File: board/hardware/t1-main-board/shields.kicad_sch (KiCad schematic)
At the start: 3 parts

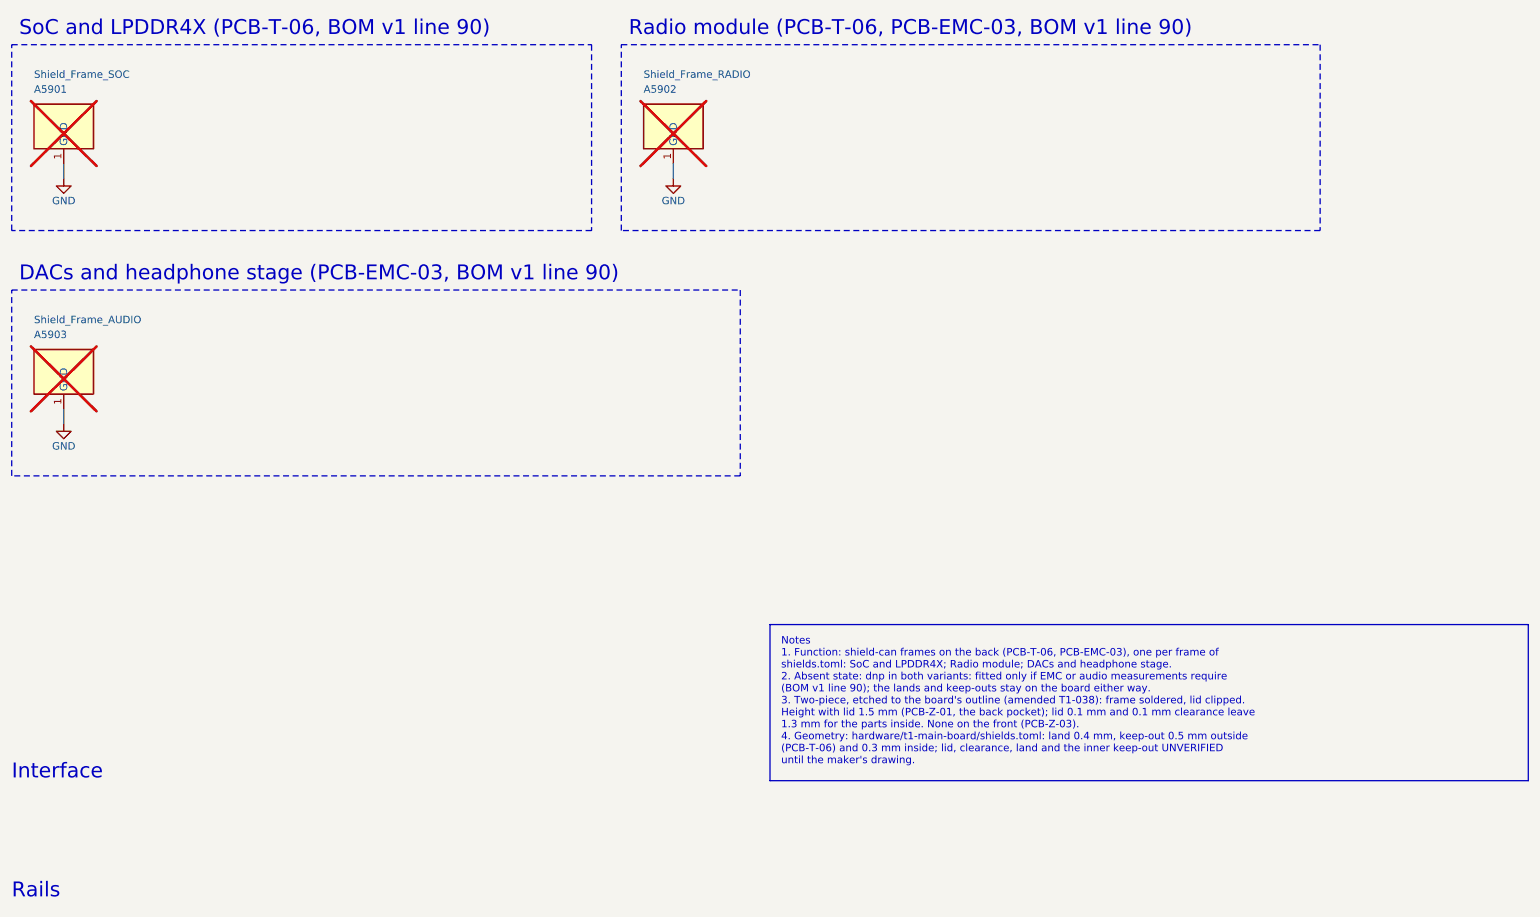
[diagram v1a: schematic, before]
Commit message: Schematic: side-pin grounds drop below their pin; shield frames in one group
A ground on an IC's side pin whose next row is taken (U1201 MODE/SYNC on
blk.vdd-cpu, U2801 VNEG/FBN on blk.hpa-rails-pre) leaves on a stub past
its neighbours' text and drops to the first free row, its GND symbol
pointing down below the pin instead of hanging among the neighbours'
labels (CRAFT-85); a ground below it on the same side joins the drop.
The shield-can frames share one group sized from its contents
(CRAFT-174) instead of three groups as wide as their titles. Other
sheets change only in #PWR numbering.

Generated twice, identical. ERC 0 errors (9 warnings, as before), craft
Q1 met (Q2 reached), overlaps 0 collisions; both sheets checked on
200 dpi PDF crops. References unchanged, so the board is not rebuilt.

Co-Authored-By: Claude Opus 5.5 <noreply@anthropic.com>
Claude-Session: https://claude.ai/code/session_013P6pW9LdyEMFishwCcZGUr
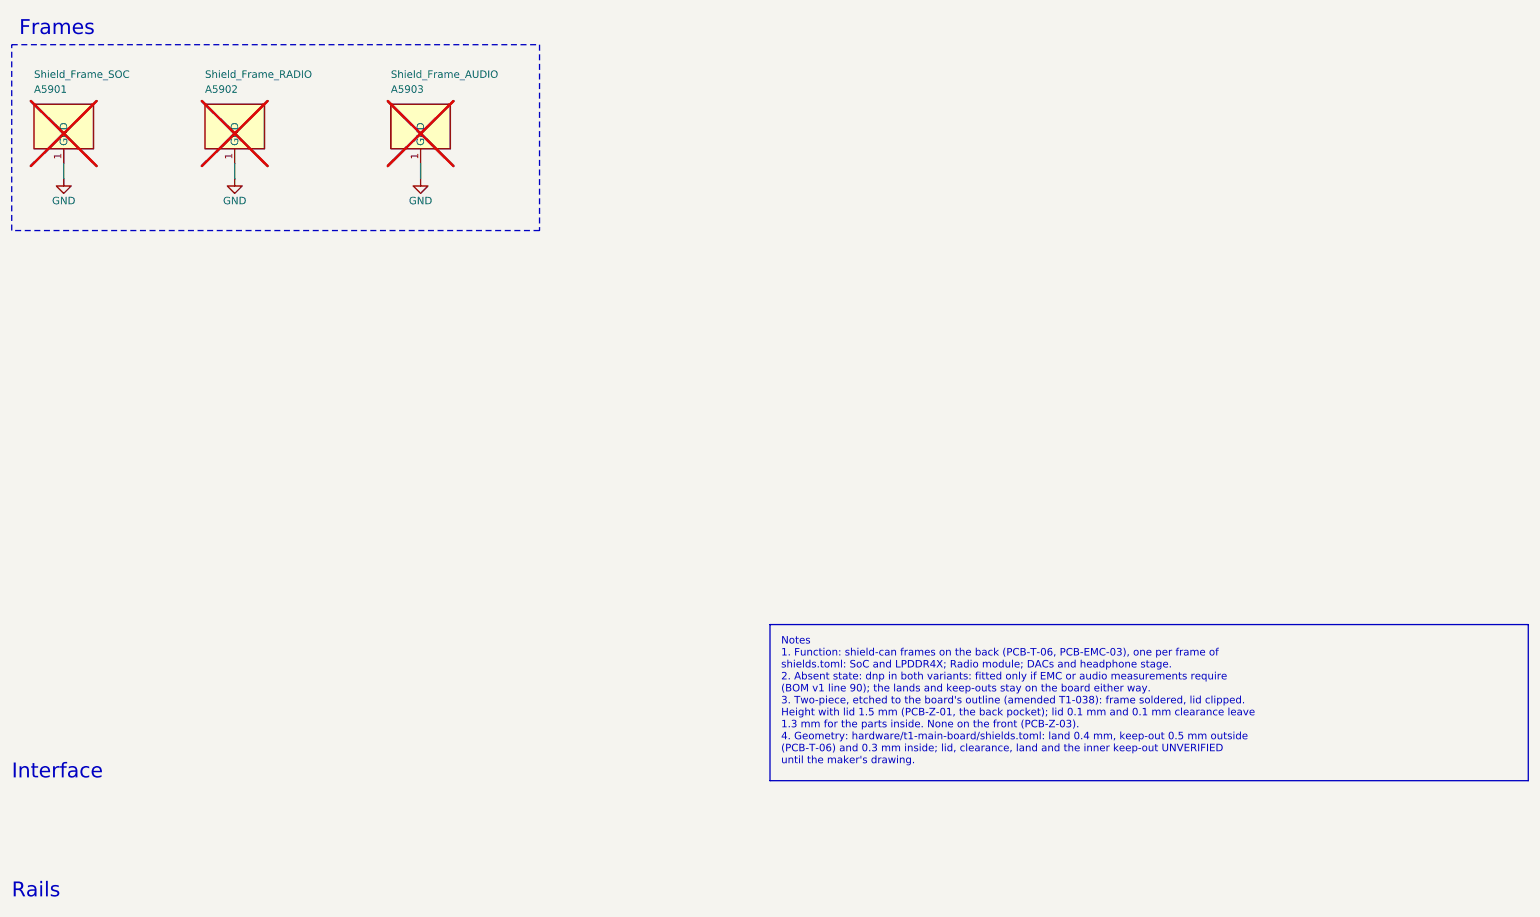
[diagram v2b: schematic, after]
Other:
- note added: "Frames"
- note removed: "DACs and headphone stage (PCB-EMC-03, BOM v1 line 90)"
- note removed: "Radio module (PCB-T-06, PCB-EMC-03, BOM v1 line 90)"
- note removed: "SoC and LPDDR4X (PCB-T-06, BOM v1 line 90)"
- moved on the sheet: A5902, A5903

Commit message: Audio shield frame dropped for board area (BOM v1.20, placement v1.7)
Maintainer decision 2026-10-28: most of the headphone stage stands on
the front, where PCB-Z-03 allows no can, so the back frame A5903 covered
little of it. PCB-T-06 asks for frames around the SoC/DDR and the radio,
so A5901 and A5902 stay; the SoC frame already encloses only the RK3566
and LPDDR4X with 0.5 mm, so it is not shrunk. PCB-EMC-03 withdraws its
headphone-stage frame (constraints v0.19); placement decision 16.

pcb/build.py --drc: 993 parts placed (716 front, 277 back), board need
99.7 % -> 98.9 %, placed courtyard 61.0 % -> 60.2 %, factor 1.64 -> 1.66;
DRC 0 errors (605 warnings, 499 unconnected, as before), ERC 0 errors,
craft Q1 met, overlaps 0, pcb tests pass (34, with the PCB-T-06 frame
set), capacitor proximity 244 within bound. Audio-zone back plot at
300 dpi compared with v1.6; shields sheet on a 200 dpi crop.
References unchanged.

Co-Authored-By: Claude Opus 5.5 <noreply@anthropic.com>
Claude-Session: https://claude.ai/code/session_013P6pW9LdyEMFishwCcZGUr
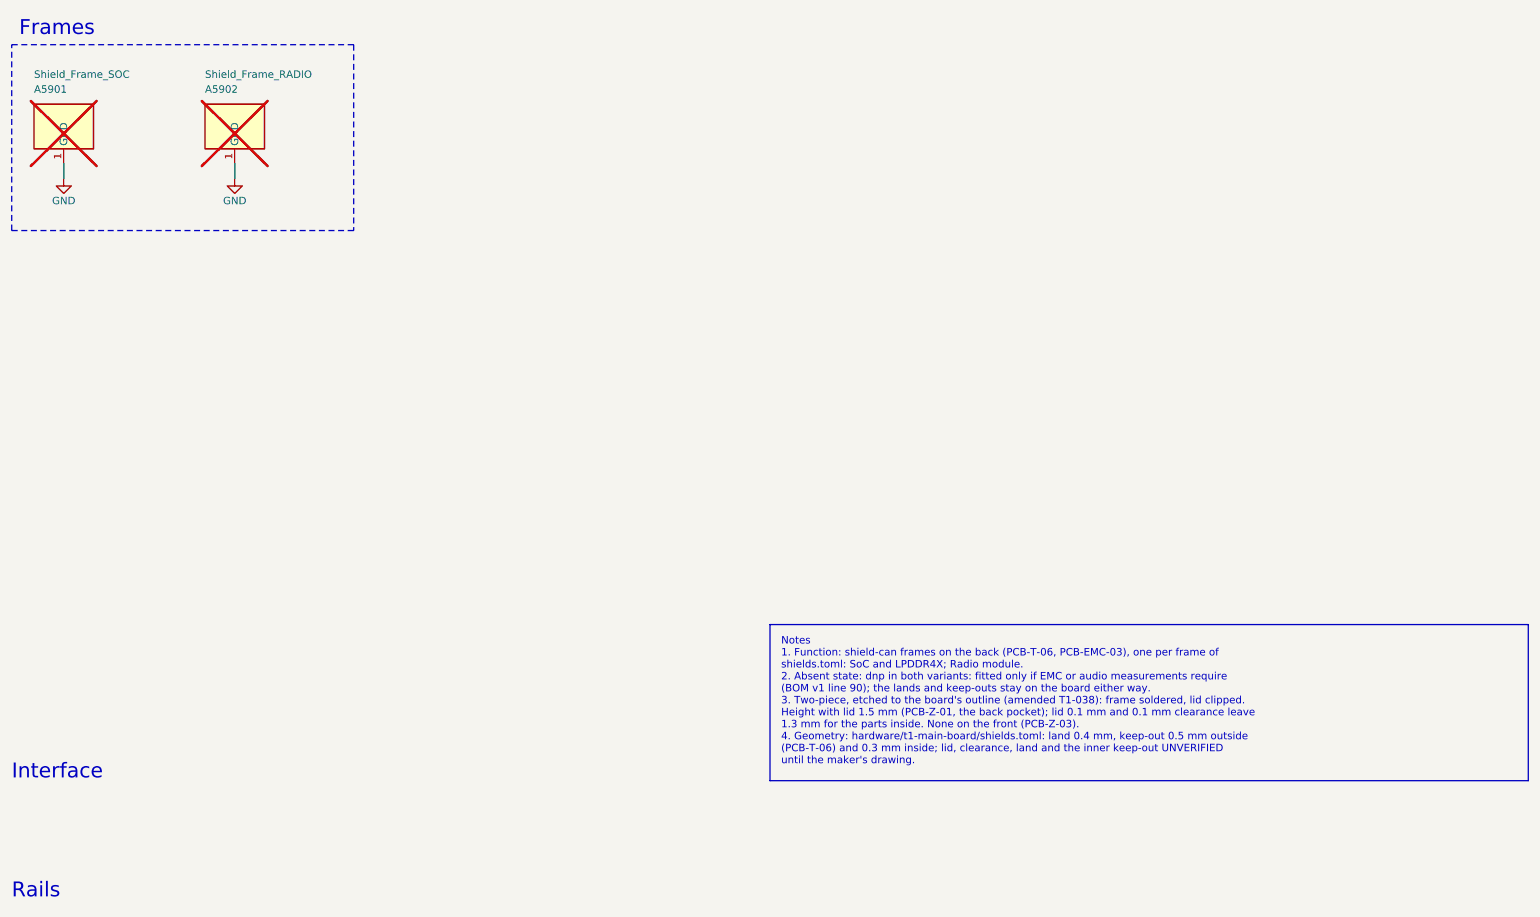
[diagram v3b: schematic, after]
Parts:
- removed A5903: Shield_Frame_AUDIO, T1_Main_Board:Shield_Frame_AUDIO_17.2x19.4mm, symbol T1_Main_Board:Shield_Frame
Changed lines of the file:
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@@
 (kicad_sch (version 20260306) (generator "eeschema") (generator_version "10.0")
 (paper "A4")
-(title_block (title "Shield-can frames") (date "2026-10-25") (rev "A") (company "The OpenDAP Project") (comment 1 "blk.shields") (comment 2 "Etched two-piece shield-can frames on the back: SoC and LPDDR4X, radio, DACs and headphone stage (not fitted)"))
+(title_block (title "Shield-can frames") (date "2026-10-25") (rev "A") (company "The OpenDAP Project") (comment 1 "blk.shields") (comment 2 "Etched two-piece shield-can frames on the back: SoC and LPDDR4X, radio module (not fitted)"))
 (symbol (lib_id "T1_Main_Board:Shield_Frame") (at 31.75 48.26 0) (unit 1) (body_style 1) (exclude_from_sim no) (in_bom yes) (on_board yes) (dnp yes)
   (property "Reference" "A5901" (at 26.67 43.18 0) (effects (font (size 1.27 1.27)) (justify left)))
@@
   (instances (project "t1-main-board" (path "/7746052e-d7f9-59ad-ba73-bd2b74439529/fe47a45a-600c-5b5b-9165-806f46ec6c77" (reference "#PWR0947") (unit 1))))
 )
-(symbol (lib_id "T1_Main_Board:Shield_Frame") (at 92.71 48.26 0) (unit 1) (body_style 1) (exclude_from_sim no) (in_bom yes) (on_board yes) (dnp yes)
-  (property "Reference" "A5903" (at 87.63 43.18 0) (effects (font (size 1.27 1.27)) (justify left)))
-  (property "Value" "Shield_Frame_AUDIO" (at 87.63 40.64 0) (effects (font (size 1.27 1.27)) (justify left)))
-  (property "Footprint" "T1_Main_Board:Shield_Frame_AUDIO_17.2x19.4mm" (at 92.71 48.26 0) (effects (font (size 1.27 1.27))) (hide yes))
-  (property "Datasheet" "https://github.com/opendap-project/board/blob/main/hardware/t1-main-board/shields.toml" (at 92.71 48.26 0) (effects (font (size 1.27 1.27))) (hide yes))
-  (property "Description" "Shield-can frame AUDIO, two-piece etched (frame + lid), 17.2 x 19.4 mm land outside, 1.5 mm with the lid, parts inside up to 1.3 mm; made to order (T1-038)" (at 92.71 48.26 0) (effects (font (size 1.27 1.27))) (hide yes))
-  (property "Manufacturer" "Made to order (etched)" (at 92.71 48.26 0) (effects (font (size 1.27 1.27))) (hide yes))
-  (property "MPN" "T1-SHIELD-AUDIO" (at 92.71 48.26 0) (effects (font (size 1.27 1.27))) (hide yes))
-  (property "Block" "blk.shields" (at 92.71 48.26 0) (effects (font (size 1.27 1.27))) (hide yes))
-  (property "Alternate" "shield-fit" (at 92.71 48.26 0) (effects (font (size 1.27 1.27))) (hide yes))
-  (pin "1")
-  (instances (project "t1-main-board" (path "/7746052e-d7f9-59ad-ba73-bd2b74439529/fe47a45a-600c-5b5b-9165-806f46ec6c77" (reference "A5903") (unit 1) (variant (name "production") (dnp yes)))))
-)
-(wire (pts (xy 92.71 55.88) (xy 92.71 58.42)) (stroke (width 0) (type default)))
-(symbol (lib_id "power:GND") (at 92.71 58.42 0) (unit 1) (body_style 1) (exclude_from_sim no) (in_bom yes) (on_board yes) (dnp no)
-  (property "Reference" "#PWR0948" (at 92.71 58.42 0) (effects (font (size 1.27 1.27))) (hide yes))
-  (property "Value" "GND" (at 92.71 62.23 0) (effects (font (size 1.27 1.27))))
-  (property "Footprint" "" (at 92.71 58.42 0) (effects (font (size 1.27 1.27))) (hide yes))
-  (property "Datasheet" "" (at 92.71 58.42 0) (effects (font (size 1.27 1.27))) (hide yes))
-  (pin "1")
-  (instances (project "t1-main-board" (path "/7746052e-d7f9-59ad-ba73-bd2b74439529/fe47a45a-600c-5b5b-9165-806f46ec6c77" (reference "#PWR0948") (unit 1))))
-)
-(rectangle (start 22.86 35.56) (end 113.03 67.31) (stroke (width 0) (type dash)) (fill (type none)))
+(rectangle (start 22.86 35.56) (end 81.28 67.31) (stroke (width 0) (type dash)) (fill (type none)))
 (text "Frames" (exclude_from_sim no) (at 24.13 34.29 0) (effects (font (size 2.54 2.54)) (justify left bottom)))
-(text_box "Notes\n1. Function: shield-can frames on the back (PCB-T-06, PCB-EMC-03), one per frame of\n   shields.toml: SoC and LPDDR4X; Radio module; DACs and headphone stage.\n2. Absent state: dnp in both variants: fitted only if EMC or audio measurements require\n   (BOM v1 line 90); the lands and keep-outs stay on the board either way.\n3. Two-piece, etched to the board's outline (amended T1-038): frame soldered, lid clipped.\n   Height with lid 1.5 mm (PCB-Z-01, the back pocket); lid 0.1 mm and 0.1 mm clearance leave\n   1.3 mm for the parts inside. None on the front (PCB-Z-03).\n4. Geometry: hardware/t1-main-board/shields.toml: land 0.4 mm, keep-out 0.5 mm outside\n   (PCB-T-06) and 0.3 mm inside; lid, clearance, land and the inner keep-out UNVERIFIED\n   until the maker's drawing." (exclude_from_sim no) (at 152.4 134.62 0) (size 129.54 26.67) (margins 1.905 1.905 1.905 1.905) (stroke (width 0) (type default)) (fill (type none)) (effects (font (size 1.27 1.27)) (justify left top)))
+(text_box "Notes\n1. Function: shield-can frames on the back (PCB-T-06, PCB-EMC-03), one per frame of\n   shields.toml: SoC and LPDDR4X; Radio module.\n2. Absent state: dnp in both variants: fitted only if EMC or audio measurements require\n   (BOM v1 line 90); the lands and keep-outs stay on the board either way.\n3. Two-piece, etched to the board's outline (amended T1-038): frame soldered, lid clipped.\n   Height with lid 1.5 mm (PCB-Z-01, the back pocket); lid 0.1 mm and 0.1 mm clearance leave\n   1.3 mm for the parts inside. None on the front (PCB-Z-03).\n4. Geometry: hardware/t1-main-board/shields.toml: land 0.4 mm, keep-out 0.5 mm outside\n   (PCB-T-06) and 0.3 mm inside; lid, clearance, land and the inner keep-out UNVERIFIED\n   until the maker's drawing." (exclude_from_sim no) (at 152.4 134.62 0) (size 129.54 26.67) (margins 1.905 1.905 1.905 1.905) (stroke (width 0) (type default)) (fill (type none)) (effects (font (size 1.27 1.27)) (justify left top)))
 (text "Rails" (exclude_from_sim no) (at 22.86 181.61 0) (effects (font (size 2.54 2.54)) (justify left bottom)))
 (table (column_count 3) (border (external yes) (header yes) (stroke (width 0) (type solid))) (separators (rows yes) (cols yes) (stroke (width 0) (type solid))) (column_widths 27.94 39.37 54.61) (row_heights 5.08 5.08) (cells (table_cell "Rail" (exclude_from_sim no) (at 22.86 182.88 0) (size 27.94 5.08) (margins 0.9525 0.9525 0.9525 0.9525) (span 1 1) (fill (type none)) (effects (font (size 1.27 1.27) (bold yes)) (justify left top))) (table_cell "Capacitors" (exclude_from_sim no) (at 50.8 182.88 0) (size 39.37 5.08) (margins 0.9525 0.9525 0.9525 0.9525) (span 1 1) (fill (type none)) (effects (font (size 1.27 1.27) (bold yes)) (justify left top))) (table_cell "Requirement and source" (exclude_from_sim no) (at 90.17 182.88 0) (size 54.61 5.08) (margins 0.9525 0.9525 0.9525 0.9525) (span 1 1) (fill (type none)) (effects (font (size 1.27 1.27) (bold yes)) (justify left top))) (table_cell "(none)" (exclude_from_sim no) (at 22.86 187.96 0) (size 27.94 5.08) (margins 0.9525 0.9525 0.9525 0.9525) (span 1 1) (fill (type none)) (effects (font (size 1.27 1.27)) (justify left top))) (table_cell "-" (exclude_from_sim no) (at 50.8 187.96 0) (size 39.37 5.08) (margins 0.9525 0.9525 0.9525 0.9525) (span 1 1) (fill (type none)) (effects (font (size 1.27 1.27)) (justify left top))) (table_cell "No supply on this sheet" (exclude_from_sim no) (at 90.17 187.96 0) (size 54.61 5.08) (margins 0.9525 0.9525 0.9525 0.9525) (span 1 1) (fill (type none)) (effects (font (size 1.27 1.27)) (justify left top)))))
